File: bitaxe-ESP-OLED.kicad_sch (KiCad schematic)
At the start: 49 parts, among them J1 SFV30R-4STE1HLF, J2 Conn_01x06, J3 USB_C_Receptacle_USB2.0_16P, Q1 SI2307, SW1 SWITCH-SPST, SW2 SWITCH-SPST, SW3 SWITCH-SPST, SW4 SWITCH-SPST, U1 ESP32_S3R8, U2 RT9080-33GJ5, U3 AP2502KTR-G1, U4 W25Q128JV, Y1 Crystal

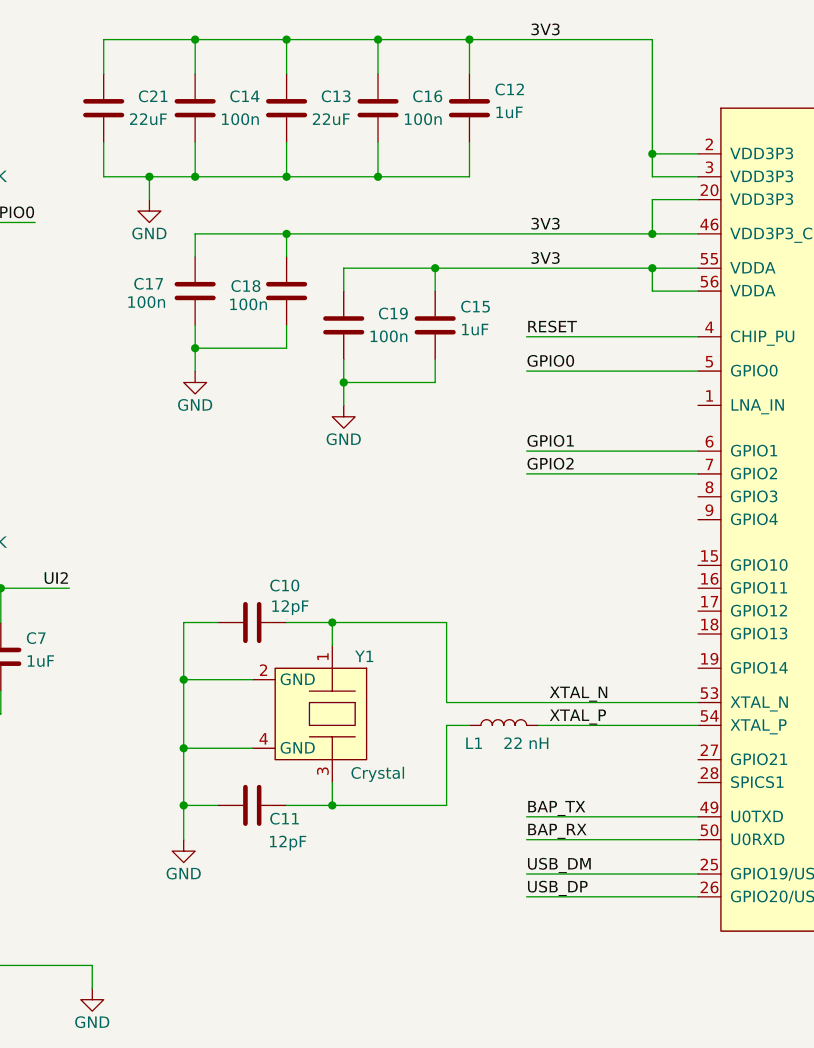
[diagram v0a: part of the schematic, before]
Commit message: main MCU routing to OLED connector
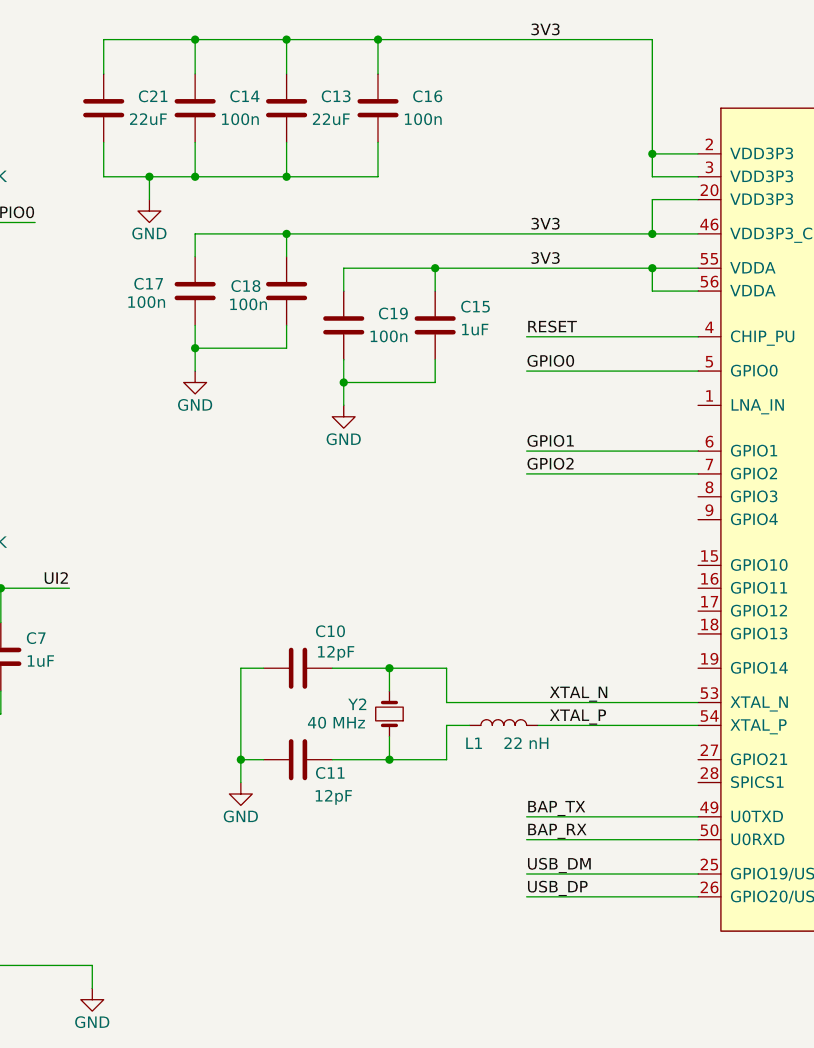
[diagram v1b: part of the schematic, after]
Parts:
- removed C12: 1uF, Capacitor_SMD:C_0402_1005Metric, symbol Device:C
- removed Y1: Crystal, symbol bitaxe:XTAL-4-pin
- added Y2: 40 MHz, bitaxe:Abracon-ABM3, symbol Device:Crystal_Small
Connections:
- net XTAL_N: now also Y2.2
- net at C11.2, L1.1: now also Y2.1
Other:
- moved on the sheet: C10, C11

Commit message: finish most of the routing
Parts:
- C9: DK 587-5514-1-ND -> 490-1550-1-ND; PARTNO EMK105BJ105MV-F -> GRM188R60J105KA01D
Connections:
- net LEDA is gone; now on net 3V3: C4.2, J1.20
- net 3V3: now also C9.1
- net LEDK1: now also J1.24; no longer J1.21
- net LEDK2: now also J1.23; no longer J1.22
- net LEDK3: now also J1.22; no longer J1.23
- net LEDK4: now also J1.21; no longer J1.24
- net UI1: now also U1.19 (GPIO14)
- net UI2: now also U1.18 (GPIO13)
- net VDD_SPI: no longer C9.1

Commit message: Finish up routing
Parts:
- removed Y2: 40 MHz, bitaxe:Abracon-ABM3, symbol Device:Crystal_Small
- added Y1: 40MHz, bitaxe:RH100-oscillator, symbol Device:Crystal_GND24
- U1: footprint Package_DFN_QFN:QFN-56-1EP_7x7mm_P0.4mm_EP4x4mm_ThermalVias -> bitaxe:QFN-56-1EP_7x7mm_P0.4mm_EP4x4mm_ThermalVias
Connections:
- net GND: now also Y1.2, Y1.4
- net XTAL_N: now also Y1.1
- net at C11.2, L1.1: now also Y1.3
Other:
- moved on the sheet: C10, C11

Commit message: commit version 0.1
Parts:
- added J3: TC2030-IDC, Connector:Tag-Connect_TC2030-IDC-NL_2x03_P1.27mm_Vertical, symbol bitaxe:TC2030-IDC-NL
- added TP1, TP10, TP11, TP13, TP2, TP3, TP4, TP5, TP6, TP7, TP8, TP9: TestPoint, TestPoint:TestPoint_Pad_D1.0mm, symbol Connector:TestPoint
- renumbered C5 to C1, C18 to C10, C19 to C11, C16 to C12, C15 to C13, C2 to C14, C1 to C15, C3 to C16, C9 to C17, C4 to C18, C8 to C19, C6 to C2, C7 to C3, C21 to C4, C14 to C5, C17 to C6, C10 to C7, C11 to C8, C13 to C9, D2 to D1, J2 to J1, J3 to J2, J1 to J4, R4 to R1, R6 to R2, R5 to R3, R7 to R4, R2 to R5, R3 to R6, R1 to R7, SW3 to SW2, SW2 to SW3, U2 to U1, U1 to U2
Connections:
- net +5V: now also TP11.1
- net 3V3: now also J3.2 (Pin_2), TP8.1
- net BAP_RX: now also U2.16 (GPIO11), TP2.1; no longer U2.50 (U0RXD)
- net BAP_TX: now also U2.15 (GPIO10), TP1.1; no longer U2.49 (U0TXD)
- net GND: now also J3.4 (Pin_4), TP10.1
- net GPIO0: now also J3.6 (Pin_6), TP9.1
- net GPIO1: now also TP3.1
- net GPIO2: now also TP4.1
- net LCD_BLK: now also U2.43 (GPIO38), TP13.1
- net RESET: now also J3.1 (Pin_1), TP5.1
- net TP_RESET: now also U2.27 (GPIO21); no longer U2.43 (GPIO38)
- new net P_RX: J3.5 (Pin_5), TP7.1, U2.50 (GPIO44/U0RXD)
- new net P_TX: J3.3 (Pin_3), TP6.1, U2.49 (GPIO43/U0TXD)
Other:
- note added: "Tag Connect"
- title: (none) -> Bitaxe ESP-OLED
- moved on the sheet: J1

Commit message: more fpc room
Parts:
- H1, H2, H3, H4: footprint MountingHole:MountingHole_3.2mm_M3_Pad_Via -> MountingHole:MountingHole_3mm_Pad_Via
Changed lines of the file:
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@@
 			)
 		)
-		(property "Footprint" "MountingHole:MountingHole_3.2mm_M3_Pad_Via"
+		(property "Footprint" "MountingHole:MountingHole_3mm_Pad_Via"
 			(at 241.3 160.02 0)
 			(effects
@@
 			)
 		)
-		(property "Footprint" "MountingHole:MountingHole_3.2mm_M3_Pad_Via"
+		(property "Footprint" "MountingHole:MountingHole_3mm_Pad_Via"
 			(at 262.89 153.67 0)
 			(effects
@@
 			)
 		)
-		(property "Footprint" "MountingHole:MountingHole_3.2mm_M3_Pad_Via"
+		(property "Footprint" "MountingHole:MountingHole_3mm_Pad_Via"
 			(at 262.89 160.02 0)
 			(effects
@@
 			)
 		)
-		(property "Footprint" "MountingHole:MountingHole_3.2mm_M3_Pad_Via"
+		(property "Footprint" "MountingHole:MountingHole_3mm_Pad_Via"
 			(at 241.3 153.67 0)
 			(effects
